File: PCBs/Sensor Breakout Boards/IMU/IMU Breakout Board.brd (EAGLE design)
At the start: 25.4 x 25.4 mm, 5 parts, among them J1 2X6 FEMALE, U1 ICM_20649

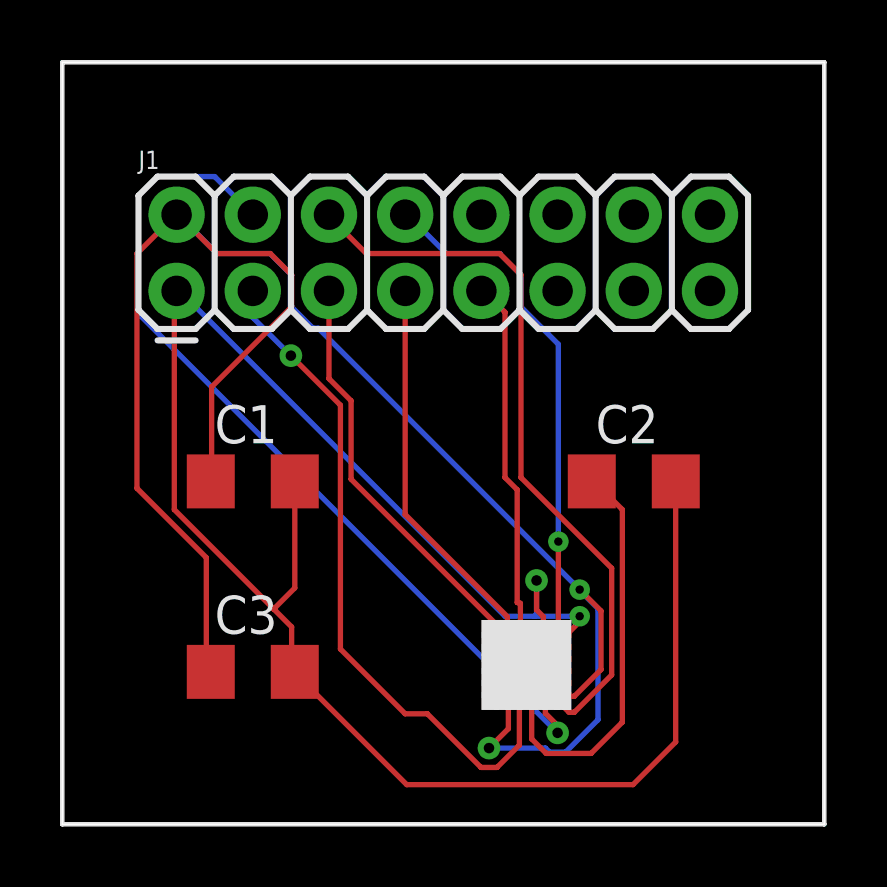
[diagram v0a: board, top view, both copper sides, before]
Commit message: rev 2 imu board complete
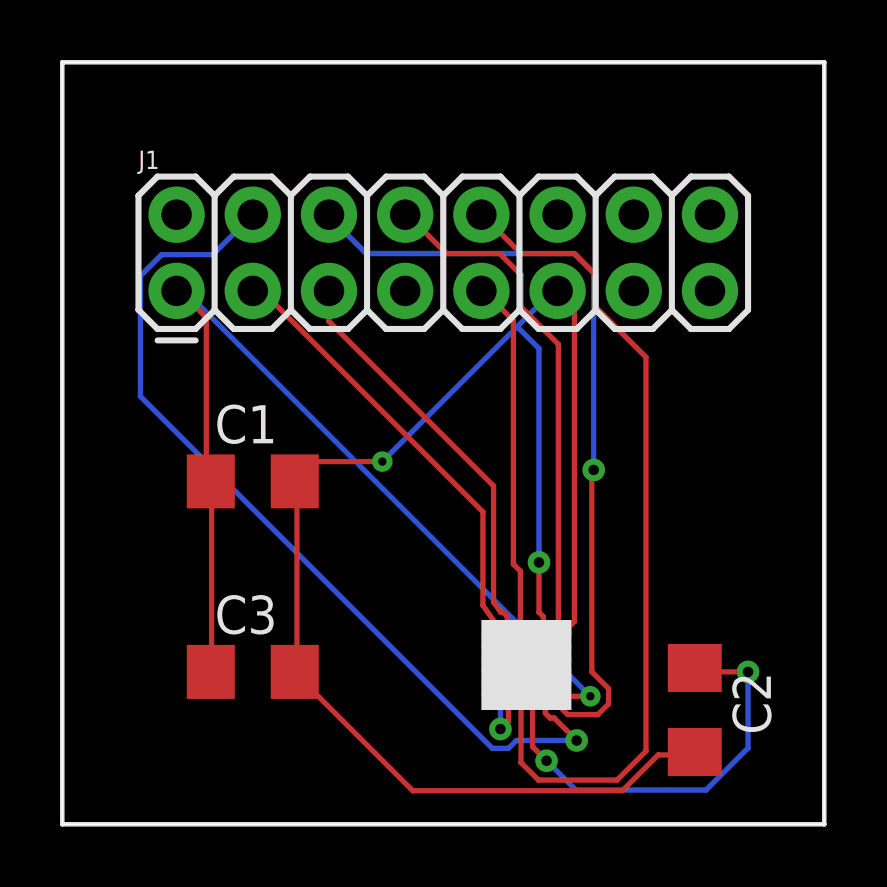
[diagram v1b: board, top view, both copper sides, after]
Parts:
- moved C2 7.89 mm to (21.1, 3.81), turned to 270 degrees
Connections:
- net N$11: now also J1.11; no longer J1.1
- net N$5: now also J1.3, U1.P11; no longer J1.7, U1.P10
- net N$6: now also U1.P10; no longer U1.P11
- net N$7: now also J1.10; no longer J1.3
- net N$8: now also J1.1; no longer J1.2
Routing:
- net N$8: track 63.6 -> 37.7 mm
- net N$11: track 64.1 -> 55.5 mm
- net N$7: track 22.4 -> 27.9 mm, vias 1 -> 0
- net N$5: track 12.5 -> 14.6 mm
- net N$2: track 24.3 -> 26.3 mm, vias 0 -> 1
- net N$9: track 13.3 -> 14.1 mm, vias 0 -> 2
- net N$3: vias 1 -> 0
